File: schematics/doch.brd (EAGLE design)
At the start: 35 x 70 mm, 37 parts, among them IC2 STM32F103C8T

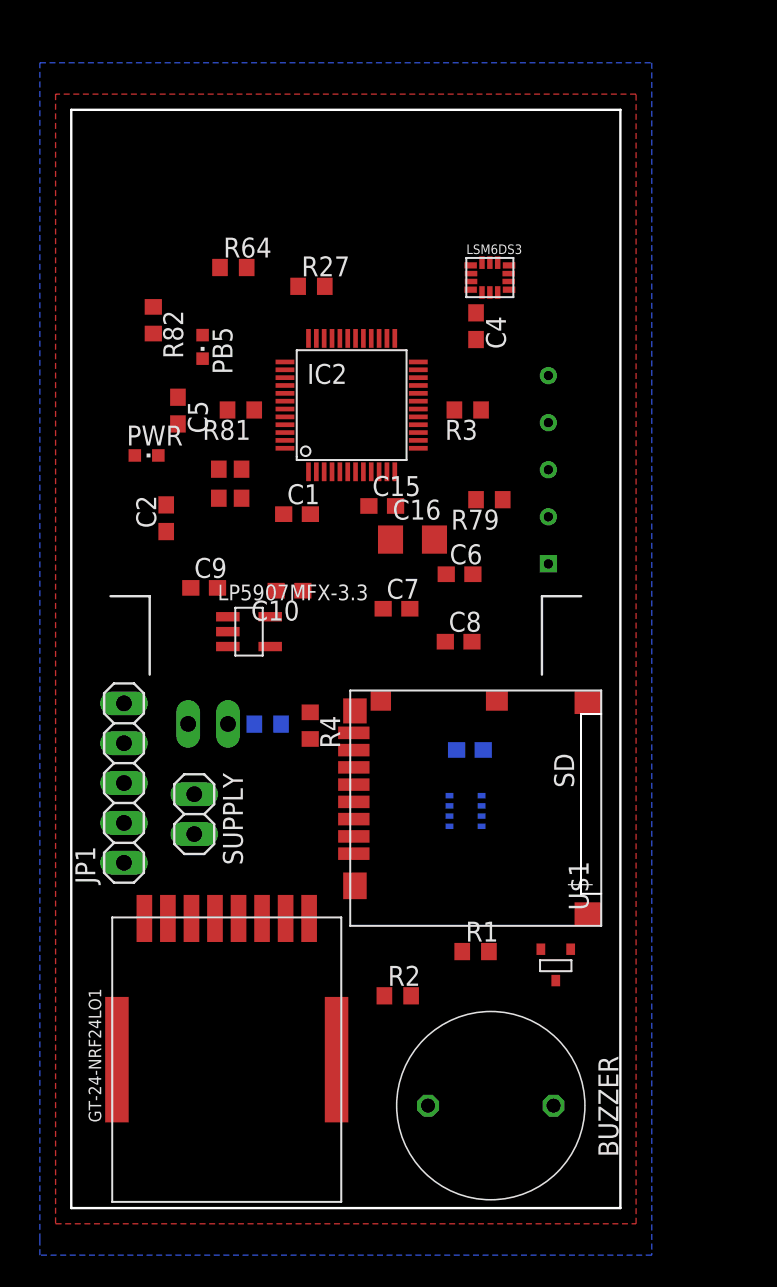
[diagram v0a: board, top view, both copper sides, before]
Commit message: Платы дочек: Новая надежда
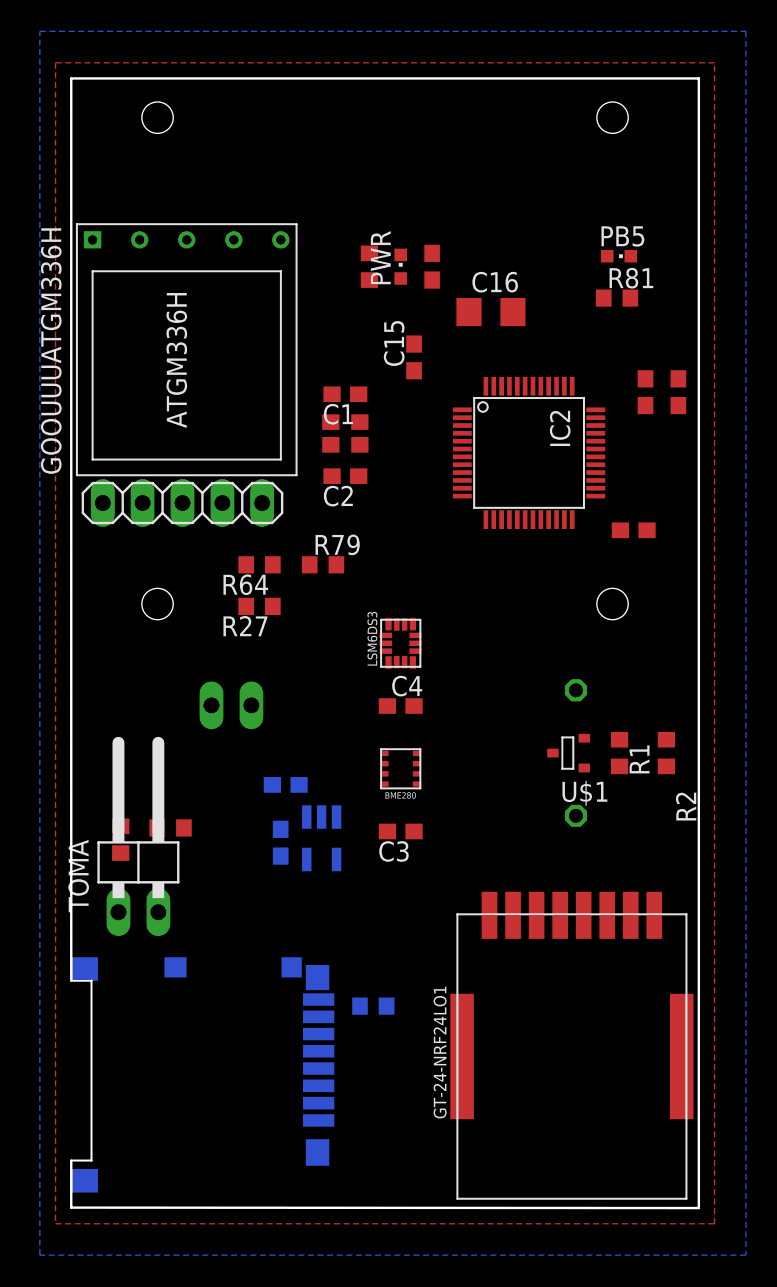
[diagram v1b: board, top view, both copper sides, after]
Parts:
- moved SD 37.8 mm to (0.00, 16.0), flipped to the bottom
- moved R3 32.7 mm to (6.33, 24.2), turned to 0 degrees
- moved PB5 27.2 mm to (34.9, 60.7), turned to 270 degrees
- moved R81 25.0 mm to (34.8, 58.0), turned to 0 degrees
- moved C4 24.7 mm to (21.0, 32.0), turned to 0 degrees
- moved LSM6DS3 24.0 mm to (21.0, 36.0), turned to 90 degrees
- moved BUZZER 23.1 mm to (32.2, 29.0), flipped to the bottom, turned to 180 degrees
- moved R2 23.1 mm to (37.9, 29.0), turned to 270 degrees
- moved GT-24-NRF24LO1 22.0 mm to (31.9, 9.66)
- moved C8 21.2 mm to (38.7, 52.0), turned to 270 degrees
- moved C7 21.0 mm to (36.6, 52.0), turned to 270 degrees
- moved R27 20.7 mm to (12.0, 38.4), turned to 180 degrees
- moved PWR 20.2 mm to (21.0, 60.0), turned to 0 degrees
- moved R64 19.0 mm to (12.0, 41.0), turned to 180 degrees
- moved C5 18.6 mm to (23.0, 60.0), turned to 90 degrees
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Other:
- board size 35 x 70 mm -> 40 x 72 mm
